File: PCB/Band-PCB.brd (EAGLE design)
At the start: 90 x 117.9 mm, 11 parts

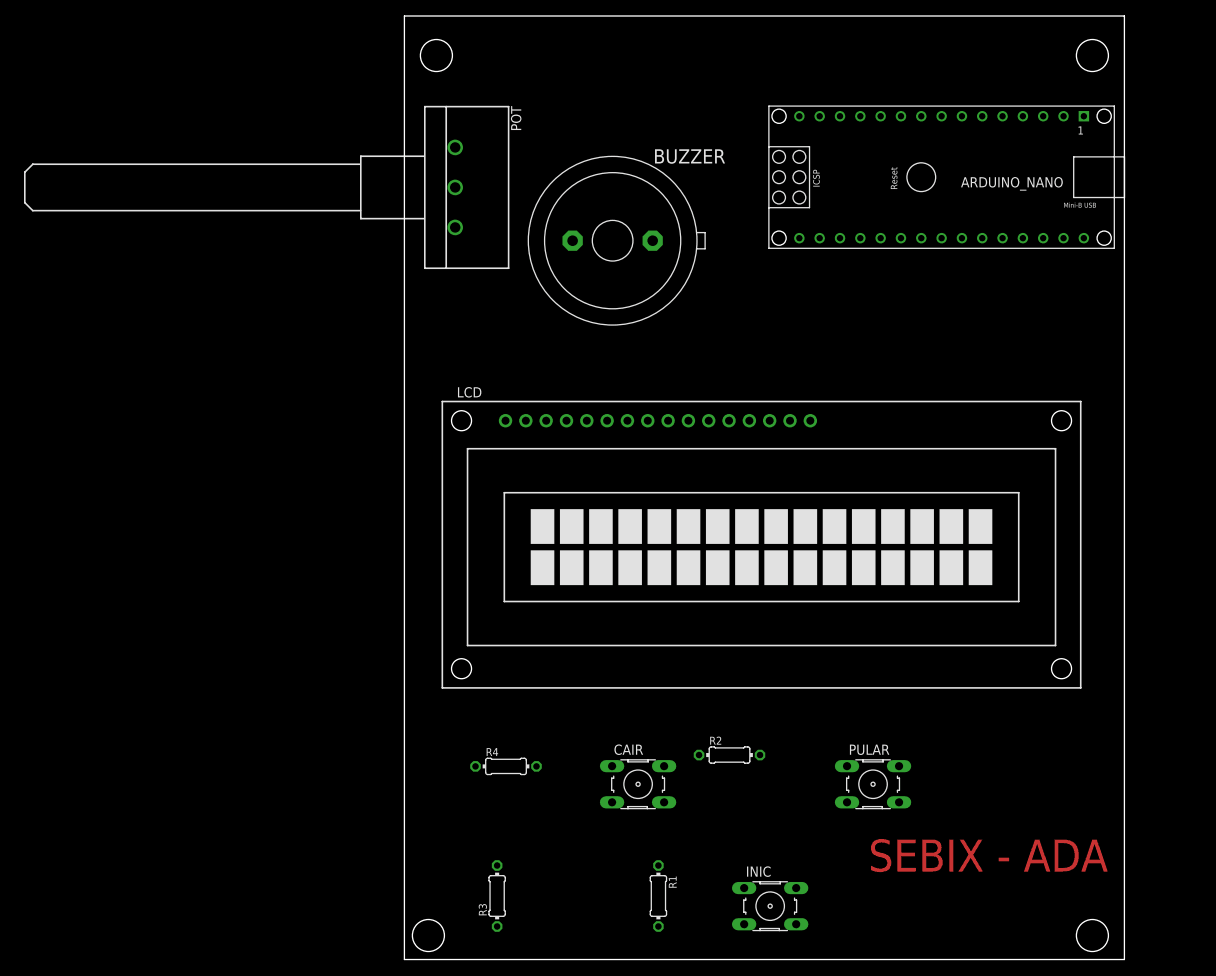
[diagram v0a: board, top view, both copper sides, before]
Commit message: PCB arrumada, tamanho 9x11 cm
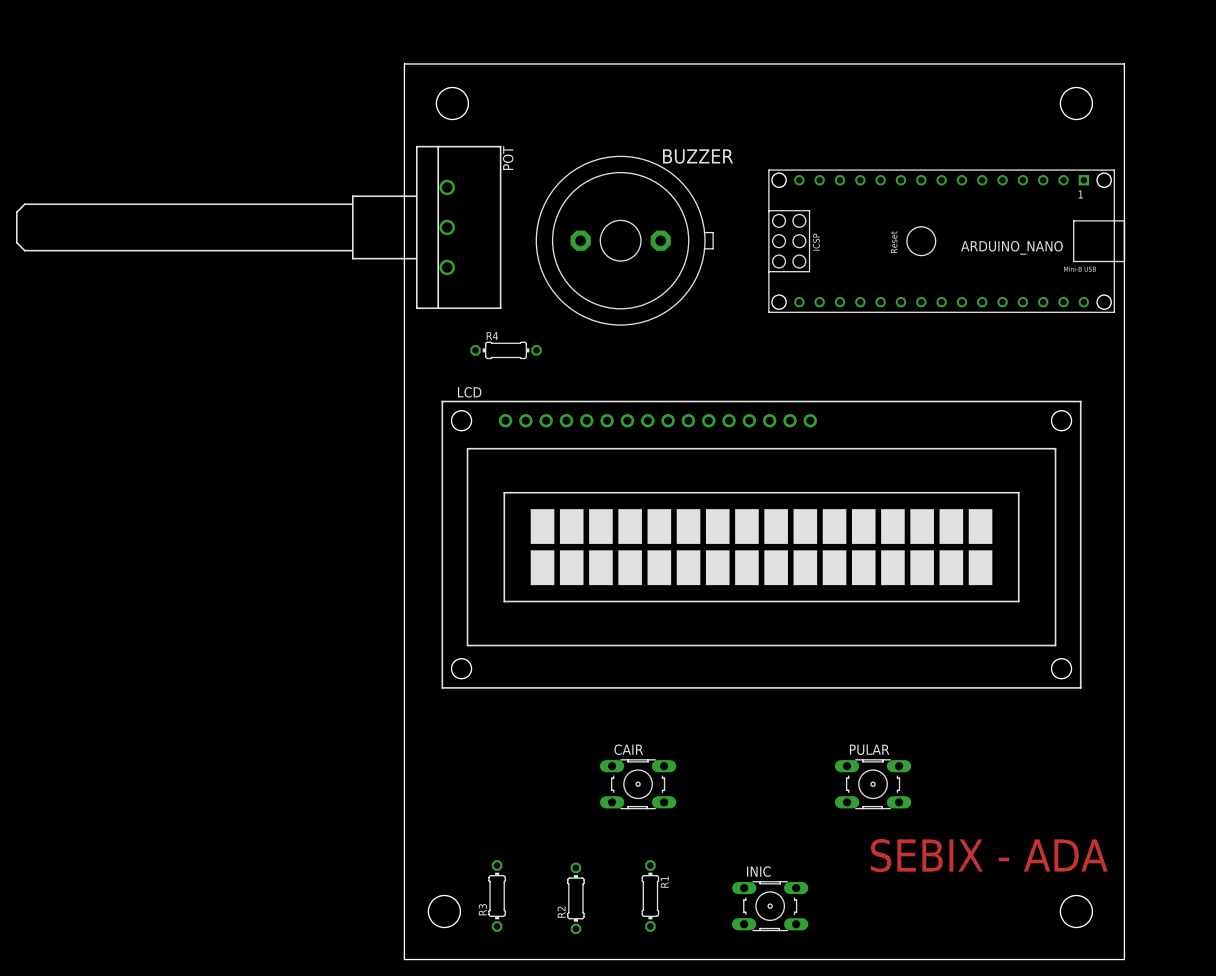
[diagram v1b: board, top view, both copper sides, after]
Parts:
- moved R4 52.0 mm to (12.7, 76.1)
- moved R2 26.3 mm to (21.4, 7.64), turned to 90 degrees
- moved ARDUINO_NANO 8.00 mm to (64.6, 89.8)
- moved POT 5.10 mm to (5.35, 91.5)
- moved BUZZER 1.00 mm to (27.0, 89.8)
- moved R1 1.00 mm to (30.8, 7.94)
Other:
- board size 90 x 117.9 mm -> 90 x 111.9 mm

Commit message: PCB feita, com rotas ligadas, 9x10cm
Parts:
- moved R2 26.4 mm to (46.6, 15.6), turned to 0 degrees
- moved R1 12.0 mm to (18.8, 6.94)
- moved R3 10.6 mm to (4.59, 15.9)
- moved PULAR 9.22 mm to (65.6, 15.9)
- moved POT 9.00 mm to (5.35, 82.5)
- moved BUZZER 8.25 mm to (29.0, 81.8)
- moved R4 8.06 mm to (16.7, 69.1)
- moved ARDUINO_NANO 7.07 mm to (63.6, 82.8)
- moved LCD 6.08 mm to (45.6, 45.9)
- moved CAIR 6.00 mm to (29.2, 15.9)
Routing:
- net VCC: track 0.00 -> 256.5 mm
- net GND: track 0.00 -> 190.0 mm
- net N$3: track 0.00 -> 135.4 mm
- net N$14: track 0.00 -> 97.6 mm
- net N$2: track 0.00 -> 94.4 mm
- net N$11: track 0.00 -> 78.6 mm
- net N$1: track 0.00 -> 77.2 mm
- net N$4: track 0.00 -> 72.1 mm
- net N$12: track 0.00 -> 57.4 mm
- net N$8: track 0.00 -> 30.5 mm
- net N$9: track 0.00 -> 30.3 mm
- net N$10: track 0.00 -> 30.3 mm
- net N$6: track 0.00 -> 24.3 mm
- net N$7: track 0.00 -> 23.9 mm
- net N$15: track 0.00 -> 19.0 mm
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- added copper zone on layer 16, net GND
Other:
- board size 90 x 111.9 mm -> 90 x 100.9 mm
